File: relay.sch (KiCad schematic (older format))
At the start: 3 parts, among them Q1 Q_NPN_BCE

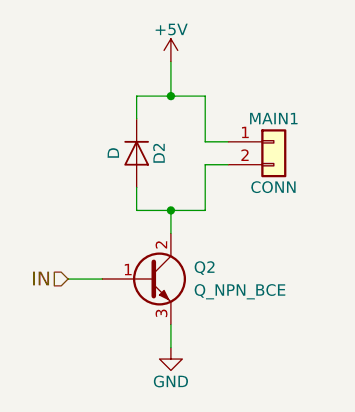
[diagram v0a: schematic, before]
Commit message: Deduping kty_84 sheet names.
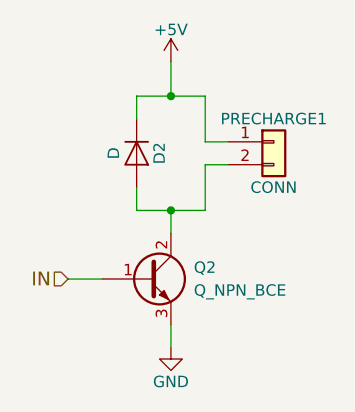
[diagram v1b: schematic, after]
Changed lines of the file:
@@
 	5550 4000 5400 4000
 $Comp
-L +5V #PWR81
+L +5V #PWR088
 U 1 1 5B006F20
 P 5850 3050
-AR Path="/5AFF2F49/5AFF30F9/5B006F20" Ref="#PWR81"  Part="1"
-AR Path="/5AFF2F49/5AFF3733/5B006F20" Ref="#PWR83"  Part="1"
-F 0 "#PWR83" H 5850 2900 50  0001 C CNN
+AR Path="/5AFF2F49/5AFF30F9/5B006F20" Ref="#PWR088"  Part="1"
+AR Path="/5AFF2F49/5AFF3733/5B006F20" Ref="#PWR090"  Part="1"
+F 0 "#PWR090" H 5850 2900 50  0001 C CNN
 F 1 "+5V" H 5850 3190 50  0000 C CNN
 F 2 "" H 5850 3050 50  0001 C CNN
@@
 $EndComp
 $Comp
-L GND #PWR82
+L GND #PWR089
 U 1 1 5B006F38
 P 5850 4300
-AR Path="/5AFF2F49/5AFF30F9/5B006F38" Ref="#PWR82"  Part="1"
-AR Path="/5AFF2F49/5AFF3733/5B006F38" Ref="#PWR84"  Part="1"
-F 0 "#PWR84" H 5850 4050 50  0001 C CNN
+AR Path="/5AFF2F49/5AFF30F9/5B006F38" Ref="#PWR089"  Part="1"
+AR Path="/5AFF2F49/5AFF3733/5B006F38" Ref="#PWR091"  Part="1"
+F 0 "#PWR091" H 5850 4050 50  0001 C CNN
 F 1 "GND" H 5850 4150 50  0000 C CNN
 F 2 "" H 5850 4300 50  0001 C CNN
@@
 AR Path="/5AFF2F49/5AFF30F9/5B007450" Ref="PRECHARGE1"  Part="1"
 AR Path="/5AFF2F49/5AFF3733/5B007450" Ref="MAIN1"  Part="1"
-F 0 "MAIN1" H 6300 3500 50  0000 C CNN
+F 0 "PRECHARGE1" H 6300 3500 50  0000 C CNN
 F 1 "CONN" H 6300 3200 50  0000 C CNN
 F 2 "" H 6300 3400 50  0001 C CNN
